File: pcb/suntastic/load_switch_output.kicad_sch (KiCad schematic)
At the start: 6 parts, among them J1 Screw_Terminal_01x02, U6 TPS22917DBV

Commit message: add wdt
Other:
- moved on the sheet: JP21
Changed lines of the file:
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@@
   (junction (at 161.29 73.025) (diameter 0) (color 0 0 0 0)
   )
-  (junction (at 162.56 62.865) (diameter 0) (color 0 0 0 0)
+  (junction (at 161.29 62.865) (diameter 0) (color 0 0 0 0)
   )
   (wire (pts (xy 166.37 59.055) (xy 166.37 62.865))
@@
     (stroke (width 0) (type default))
   )
-  (wire (pts (xy 160.02 62.865) (xy 162.56 62.865))
+  (wire (pts (xy 160.02 62.865) (xy 161.29 62.865))
     (stroke (width 0) (type default))
   )
@@
     (stroke (width 0) (type default))
   )
-  (wire (pts (xy 162.56 62.865) (xy 166.37 62.865))
+  (wire (pts (xy 161.29 62.865) (xy 166.37 62.865))
     (stroke (width 0) (type default))
   )
-  (wire (pts (xy 165.735 44.45) (xy 162.56 44.45))
+  (wire (pts (xy 164.465 48.26) (xy 161.29 48.26))
     (stroke (width 0) (type default))
   )
-  (wire (pts (xy 162.56 44.45) (xy 162.56 62.865))
+  (wire (pts (xy 161.29 48.26) (xy 161.29 62.865))
     (stroke (width 0) (type default))
   )
@@
     (stroke (width 0) (type default))
   )
-  (wire (pts (xy 173.355 44.45) (xy 174.625 44.45))
+  (wire (pts (xy 172.085 48.26) (xy 173.355 48.26))
     (stroke (width 0) (type default))
   )
@@
     )
   )
-  (global_label "Vin_buck_boost" (shape input) (at 174.625 44.45 0) (fields_autoplaced)
+  (global_label "Vin_buck_boost" (shape input) (at 173.355 48.26 0) (fields_autoplaced)
     (effects (font (size 1.27 1.27)) (justify left))
-    (property "Intersheetrefs" "${INTERSHEET_REFS}" (at 191.9239 44.45 0)
+    (property "Intersheetrefs" "${INTERSHEET_REFS}" (at 190.6539 48.26 0)
       (effects (font (size 1.27 1.27)) (justify left) hide)
     )
@@
     )
   )
-  (symbol (lib_id "Jumper:SolderJumper_2_Open") (at 169.545 44.45 0) (unit 1)
+  (symbol (lib_id "Jumper:SolderJumper_2_Open") (at 168.275 48.26 0) (unit 1)
     (in_bom yes) (on_board yes) (dnp no) (fields_autoplaced)
-    (property "Reference" "JP21" (at 169.545 39.37 0)
+    (property "Reference" "JP21" (at 168.275 43.18 0)
       (effects (font (size 1.27 1.27)))
     )
-    (property "Value" "SolderJumper_2_Open" (at 169.545 41.91 0)
+    (property "Value" "SolderJumper_2_Open" (at 168.275 45.72 0)
       (effects (font (size 1.27 1.27)))
     )
-    (property "Footprint" "" (at 169.545 44.45 0)
+    (property "Footprint" "" (at 168.275 48.26 0)
       (effects (font (size 1.27 1.27)) hide)
     )
-    (property "Datasheet" "~" (at 169.545 44.45 0)
+    (property "Datasheet" "~" (at 168.275 48.26 0)
       (effects (font (size 1.27 1.27)) hide)
     )

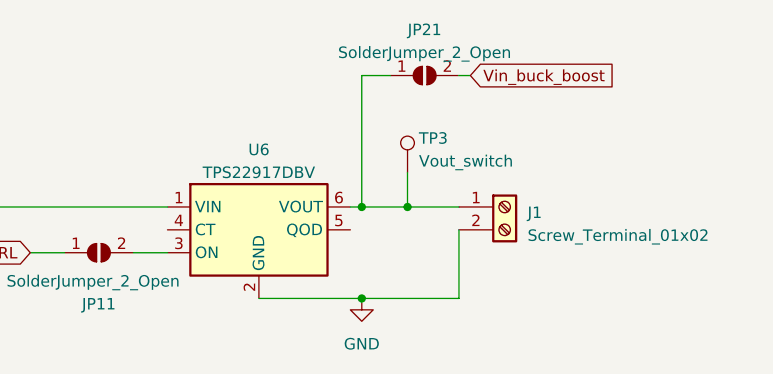
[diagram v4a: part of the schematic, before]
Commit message: Add two alternatives to obtain 3.3V for the SX chip
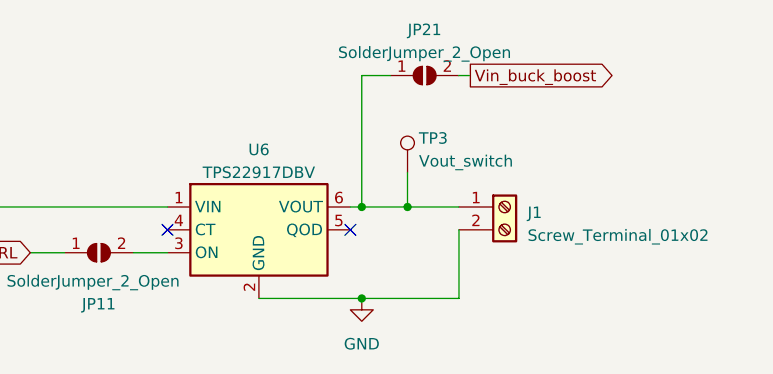
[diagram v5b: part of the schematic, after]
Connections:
- no-connect marks 0 -> 2
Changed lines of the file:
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@@
   (junction (at 161.29 62.865) (diameter 0) (color 0 0 0 0)
   )
+  (no_connect (at 139.7 65.405))
+  (no_connect (at 160.02 65.405))
   (wire (pts (xy 166.37 59.055) (xy 166.37 62.865))
     (stroke (width 0) (type default))
@@
     )
   )
-  (global_label "Vin_buck_boost" (shape input) (at 173.355 48.26 0) (fields_autoplaced)
+  (global_label "Vin_buck_boost" (shape output) (at 173.355 48.26 0) (fields_autoplaced)
     (effects (font (size 1.27 1.27)) (justify left))
     (property "Intersheetrefs" "${INTERSHEET_REFS}" (at 190.6539 48.26 0)

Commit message: Update footprints
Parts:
- JP21: footprint (none) -> Jumper:SolderJumper-2_P1.3mm_Open_RoundedPad1.0x1.5mm
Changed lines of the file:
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@@
       (effects (font (size 1.27 1.27)))
     )
-    (property "Footprint" "" (at 168.275 48.26 0)
+    (property "Footprint" "Jumper:SolderJumper-2_P1.3mm_Open_RoundedPad1.0x1.5mm" (at 168.275 48.26 0)
       (effects (font (size 1.27 1.27)) hide)
     )

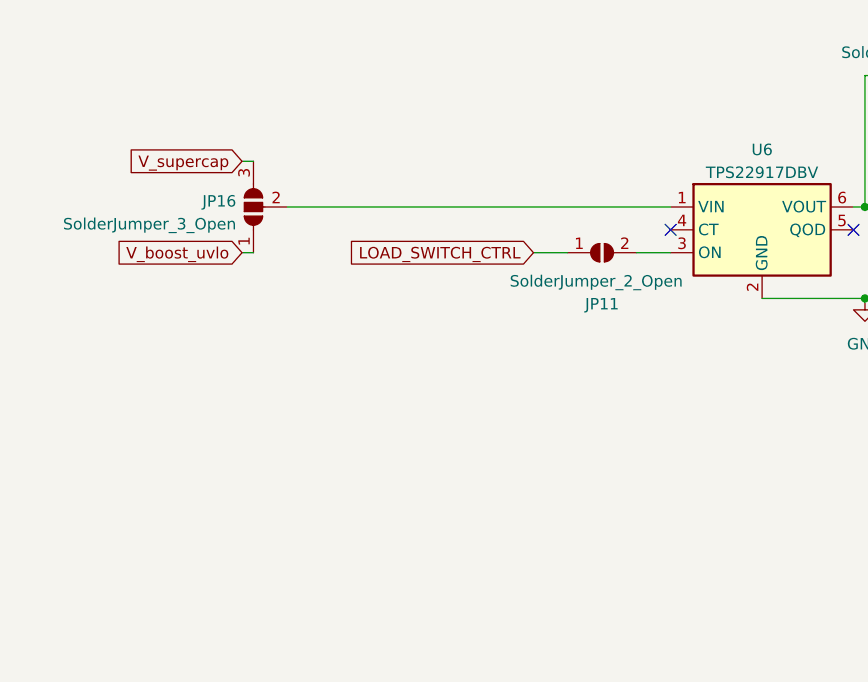
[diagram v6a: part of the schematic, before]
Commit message: Update more footprints and start with PCB
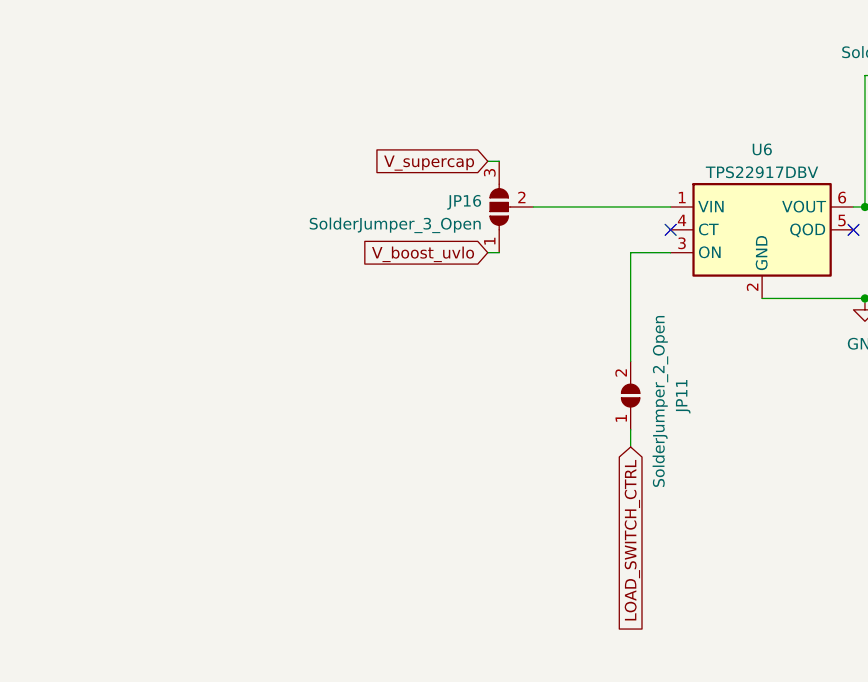
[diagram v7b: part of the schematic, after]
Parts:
- J1: footprint (none) -> TerminalBlock:TerminalBlock_bornier-2_P5.08mm
- TP3: footprint (none) -> TestPoint:TestPoint_Pad_D1.5mm
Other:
- moved on the sheet: JP11, JP16
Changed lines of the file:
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@@
     (stroke (width 0) (type default))
   )
-  (wire (pts (xy 97.155 62.865) (xy 139.7 62.865))
+  (wire (pts (xy 124.46 62.865) (xy 139.7 62.865))
     (stroke (width 0) (type default))
   )
@@
     (stroke (width 0) (type default))
   )
-  (wire (pts (xy 92.075 67.945) (xy 93.345 67.945))
+  (wire (pts (xy 119.38 67.945) (xy 120.65 67.945))
     (stroke (width 0) (type default))
   )
@@
     (stroke (width 0) (type default))
   )
-  (wire (pts (xy 92.075 57.785) (xy 93.345 57.785))
-    (stroke (width 0) (type default))
-  )
-  (wire (pts (xy 135.89 67.945) (xy 139.7 67.945))
+  (wire (pts (xy 119.38 57.785) (xy 120.65 57.785))
     (stroke (width 0) (type default))
   )
@@
     (stroke (width 0) (type default))
   )
-  (wire (pts (xy 124.46 67.945) (xy 128.27 67.945))
+  (wire (pts (xy 135.255 67.945) (xy 139.7 67.945))
+    (stroke (width 0) (type default))
+  )
+  (wire (pts (xy 135.255 89.535) (xy 135.255 87.63))
     (stroke (width 0) (type default))
   )
@@
     (stroke (width 0) (type default))
   )
-  (global_label "V_supercap" (shape input) (at 92.075 57.785 180) (fields_autoplaced)
+  (wire (pts (xy 135.255 80.01) (xy 135.255 67.945))
+    (stroke (width 0) (type default))
+  )
+  (global_label "V_supercap" (shape input) (at 119.38 57.785 180) (fields_autoplaced)
     (effects (font (size 1.27 1.27)) (justify right))
-    (property "Intersheetrefs" "${INTERSHEET_REFS}" (at 78.5255 57.785 0)
+    (property "Intersheetrefs" "${INTERSHEET_REFS}" (at 105.8305 57.785 0)
       (effects (font (size 1.27 1.27)) (justify right) hide)
     )
   )
-  (global_label "V_boost_uvlo" (shape input) (at 92.075 67.945 180) (fields_autoplaced)
+  (global_label "V_boost_uvlo" (shape input) (at 119.38 67.945 180) (fields_autoplaced)
     (effects (font (size 1.27 1.27)) (justify right))
-    (property "Intersheetrefs" "${INTERSHEET_REFS}" (at 77.0138 67.945 0)
+    (property "Intersheetrefs" "${INTERSHEET_REFS}" (at 104.3188 67.945 0)
       (effects (font (size 1.27 1.27)) (justify right) hide)
     )
@@
     )
   )
-  (global_label "LOAD_SWITCH_CTRL" (shape input) (at 124.46 67.945 180) (fields_autoplaced)
+  (global_label "LOAD_SWITCH_CTRL" (shape input) (at 135.255 89.535 270) (fields_autoplaced)
     (effects (font (size 1.27 1.27)) (justify right))
-    (property "Intersheetrefs" "${INTERSHEET_REFS}" (at 103.5323 67.945 0)
+    (property "Intersheetrefs" "${INTERSHEET_REFS}" (at 135.255 110.4627 90)
       (effects (font (size 1.27 1.27)) (justify right) hide)
     )
@@
       (effects (font (size 1.27 1.27)) (justify left))
     )
-    (property "Footprint" "" (at 171.45 59.055 0)
+    (property "Footprint" "TestPoint:TestPoint_Pad_D1.5mm" (at 171.45 59.055 0)
       (effects (font (size 1.27 1.27)) hide)
     )
@@
       (effects (font (size 1.27 1.27)) (justify left))
     )
-    (property "Footprint" "" (at 177.165 62.865 0)
+    (property "Footprint" "TerminalBlock:TerminalBlock_bornier-2_P5.08mm" (at 177.165 62.865 0)
       (effects (font (size 1.27 1.27)) hide)
     )
@@
     )
   )
-  (symbol (lib_id "Jumper:SolderJumper_2_Open") (at 132.08 67.945 0) (unit 1)
+  (symbol (lib_id "Jumper:SolderJumper_2_Open") (at 135.255 83.82 90) (unit 1)
     (in_bom yes) (on_board yes) (dnp no)
-    (property "Reference" "JP11" (at 132.08 73.66 0)
-      (effects (font (size 1.27 1.27)))
-    )
-    (property "Value" "SolderJumper_2_Open" (at 131.445 71.12 0)
-      (effects (font (size 1.27 1.27)))
-    )
-    (property "Footprint" "Jumper:SolderJumper-2_P1.3mm_Open_RoundedPad1.0x1.5mm" (at 132.08 67.945 0)
-      (effects (font (size 1.27 1.27)) hide)
-    )
-    (property "Datasheet" "~" (at 132.08 67.945 0)
+    (property "Reference" "JP11" (at 140.97 83.82 0)
+      (effects (font (size 1.27 1.27)))
+    )
+    (property "Value" "SolderJumper_2_Open" (at 138.43 84.455 0)
+      (effects (font (size 1.27 1.27)))
+    )
+    (property "Footprint" "Jumper:SolderJumper-2_P1.3mm_Open_RoundedPad1.0x1.5mm" (at 135.255 83.82 0)
+      (effects (font (size 1.27 1.27)) hide)
+    )
+    (property "Datasheet" "~" (at 135.255 83.82 0)
       (effects (font (size 1.27 1.27)) hide)
     )
@@
     )
   )
-  (symbol (lib_id "Jumper:SolderJumper_3_Open") (at 93.345 62.865 90) (unit 1)
-    (in_bom yes) (on_board yes) (dnp no) (fields_autoplaced)
-    (property "Reference" "JP16" (at 91.44 62.23 90)
-      (effects (font (size 1.27 1.27)) (justify left))
-    )
-    (property "Value" "SolderJumper_3_Open" (at 91.44 64.77 90)
-      (effects (font (size 1.27 1.27)) (justify left))
-    )
-    (property "Footprint" "Jumper:SolderJumper-3_P1.3mm_Open_RoundedPad1.0x1.5mm" (at 93.345 62.865 0)
-      (effects (font (size 1.27 1.27)) hide)
-    )
-    (property "Datasheet" "~" (at 93.345 62.865 0)
-      (effects (font (size 1.27 1.27)) hide)
-    )
+  (symbol (lib_id "Jumper:SolderJumper_3_Open") (at 120.65 62.865 90) (unit 1)
+    (in_bom yes) (on_board yes) (dnp no) (fields_autoplaced)
+    (property "Reference" "JP16" (at 118.745 62.23 90)
+      (effects (font (size 1.27 1.27)) (justify left))
+    )
+    (property "Value" "SolderJumper_3_Open" (at 118.745 64.77 90)
+      (effects (font (size 1.27 1.27)) (justify left))
+    )
+    (property "Footprint" "Jumper:SolderJumper-3_P1.3mm_Open_RoundedPad1.0x1.5mm" (at 120.65 62.865 0)
+      (effects (font (size 1.27 1.27)) hide)
+    )
+    (property "Datasheet" "~" (at 120.65 62.865 0)
+      (effects (font (size 1.27 1.27)) hide)
+    )

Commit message: Rework watchdog
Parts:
- added C11: 1uF, Capacitor_SMD:CP_Elec_4x4.5, symbol Device:C_Polarized
- added C4: 0.1uF, Capacitor_SMD:C_0603_1608Metric_Pad1.08x0.95mm_HandSolder, symbol Device:C
- added JP28: SolderJumper_2_Open, Jumper:SolderJumper-2_P1.3mm_Open_RoundedPad1.0x1.5mm, symbol Jumper:SolderJumper_2_Open
- added U10: TC7WH08FK_LJCT, Package_SO:TSSOP-8_3x3mm_P0.65mm, symbol TC7WH08FK:TC7WH08FK_LJCT
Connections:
- net GND: now also C11.2, C4.2, U10.1 (1A), U10.2 (1B), U10.4 (GND)
- net V_boost_uvlo: now also C11.1, C4.1, U10.8 (VDD)
- net at U6.3 (ON): now also U10.3 (OUT_2); no longer JP11.2 (B)
- net at U6.5 (QOD): now also JP28.1 (A)
- net at J1.1 (Pin_1), JP21.1 (A), TP3.1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: now also JP28.2 (B)
- new net: JP11.2 (B), U10.5 (2A)
- new net RST_SIGNAL: U10.6 (2B)
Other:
- moved on the sheet: JP11
